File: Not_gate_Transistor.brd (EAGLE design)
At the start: 24.3 x 22.9 mm, 8 parts, among them Q1 BC547A

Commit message: update
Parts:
- moved 5V 27.9 mm to (12.1, 33.9), turned to 180 degrees
- moved S1 14.5 mm to (9.01, 25.5), turned to 90 degrees
- moved R2 9.77 mm to (15.5, 25.7), turned to 270 degrees
- moved LED1 9.52 mm to (12.6, 12.5), turned to 270 degrees
- moved Q1 9.22 mm to (13.8, 16.6)
- moved GND 3.73 mm to (8.19, 8.05)
- moved OUTPUT 3.61 mm to (15.7, 8.00)
- moved R1 1.05 mm to (8.51, 16.3)
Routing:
- net 5V: track 26.8 -> 0.00 mm
- net GND: track 24.5 -> 0.00 mm
- net N$2: track 10.4 -> 0.00 mm
- net N$3: track 10.1 -> 0.00 mm
- net N$4: track 8.37 -> 0.00 mm
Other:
- board size 24.3 x 22.9 mm -> 22 x 40 mm
- board text added: "Pinwheel Robotics"
- board text added: "care@pinwheel.in"

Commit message: New Updates
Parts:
- moved OUTPUT 0.11 mm to (15.7, 8.10)
- moved GND 0.09 mm to (8.27, 8.09)
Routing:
- net GND: track 0.00 -> 19.1 mm
- net 5V: track 0.00 -> 16.8 mm
- net N$4: track 0.00 -> 8.89 mm
- net N$2: track 0.00 -> 7.69 mm
- net N$3: track 0.00 -> 4.05 mm
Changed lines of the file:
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@@
 <drawing>
 <settings>
-<setting alwaysvectorfont="yes"/>
+<setting alwaysvectorfont="no"/>
 <setting verticaltext="up"/>
 </settings>
@@
 <plain>
 <text x="4.516" y="14.23" size="1.778" layer="21" rot="R90">Pinwheel Robotics </text>
-<hole x="3.009" y="38.751" drill="3"/>
-<hole x="20.944" y="38.738" drill="3"/>
-<hole x="3.08" y="3.04" drill="3"/>
-<hole x="20.91" y="3.088" drill="3"/>
+<hole x="3.009" y="38.5" drill="3"/>
+<hole x="21" y="38.5" drill="3"/>
+<hole x="3" y="3.04" drill="3"/>
+<hole x="21" y="3.088" drill="3"/>
 <wire x1="1" y1="39.059846875" x2="1" y2="3.00098125" width="0.1524" layer="20"/>
 <wire x1="1" y1="3.00098125" x2="3.00098125" y2="1" width="0.1524" layer="20" curve="90"/>
@@
 <attribute name="NAME" x="9.894" y="29.673" size="0.8128" layer="21" font="vector"/>
 </element>
-<element name="GND" library="microbit" package="MICROBIT_PAD" value="MICROBIT_PAD" x="8.185" y="8.052" smashed="yes">
-<attribute name="NAME" x="5.291" y="10.194" size="0.8128" layer="21" font="vector" rot="R90"/>
+<element name="GND" library="microbit" package="MICROBIT_PAD" value="MICROBIT_PAD" x="8.266084375" y="8.092525" smashed="yes">
+<attribute name="NAME" x="5.372084375" y="10.234525" size="0.8128" layer="21" font="vector" rot="R90"/>
 </element>
 <element name="LED1" library="led" library_urn="urn:adsk.eagle:library:259" package="CHIP-LED0805" package3d_urn="urn:adsk.eagle:package:15818/2" value="" x="12.603" y="12.494" smashed="yes" rot="R270">
@@
 <attribute name="VALUE" x="11.333" y="9.954" size="1.27" layer="27"/>
 </element>
-<element name="OUTPUT" library="microbit" package="MICROBIT_PAD" value="MICROBIT_PAD" x="15.686" y="8.002" smashed="yes">
-<attribute name="NAME" x="13.4" y="11.558" size="0.8128" layer="21" font="vector"/>
+<element name="OUTPUT" library="microbit" package="MICROBIT_PAD" value="MICROBIT_PAD" x="15.73645625" y="8.102915625" smashed="yes">
+<attribute name="NAME" x="13.45045625" y="11.658915625" size="0.8128" layer="21" font="vector"/>
 </element>
 <element name="Q1" library="transistor-npn" library_urn="urn:adsk.eagle:library:398" package="TO92" package3d_urn="urn:adsk.eagle:package:28523/2" value="BC547A" x="13.843" y="16.637" smashed="yes">
@@
 <contactref element="OUTPUT" pad="PAD"/>
 <contactref element="GND" pad="PAD"/>
-<wire x1="13.653" y1="12.494" x2="15.113" y2="16.637" width="0" layer="19" extent="1-1"/>
-<wire x1="8.185" y1="8.052" x2="13.653" y2="12.494" width="0" layer="19" extent="1-1"/>
-<wire x1="15.686" y1="8.002" x2="8.185" y2="8.052" width="0" layer="19" extent="1-1"/>
+<wire x1="13.8176" y1="15.24" x2="13.8176" y2="12.5984" width="0.254" layer="1"/>
+<wire x1="15.0368" y1="16.4592" x2="13.8176" y2="15.24" width="0.254" layer="1"/>
+<wire x1="13.8176" y1="12.5984" x2="13.653" y2="12.494" width="0.254" layer="1"/>
+<wire x1="15.0368" y1="16.4592" x2="15.113" y2="16.637" width="0.254" layer="1"/>
+<wire x1="13.8176" y1="9.9568" x2="13.8176" y2="12.3952" width="0.254" layer="1"/>
+<wire x1="15.6464" y1="8.128" x2="13.8176" y2="9.9568" width="0.254" layer="1"/>
+<wire x1="13.8176" y1="12.3952" x2="13.653" y2="12.494" width="0.254" layer="1"/>
+<wire x1="15.6464" y1="8.128" x2="15.73645625" y2="8.102915625" width="0.254" layer="1"/>
+<wire x1="10.7696" y1="8.128" x2="8.3312" y2="8.128" width="0.254" layer="1"/>
+<wire x1="12.5984" y1="9.9568" x2="10.7696" y2="8.128" width="0.254" layer="1"/>
+<wire x1="13.8176" y1="9.9568" x2="12.5984" y2="9.9568" width="0.254" layer="1"/>
+<wire x1="8.3312" y1="8.128" x2="8.266084375" y2="8.092525" width="0.254" layer="1"/>
+<wire x1="13.8176" y1="9.9568" x2="15.73645625" y2="8.102915625" width="0.254" layer="1"/>
 </signal>
 <signal name="N$2">
@@
 <contactref element="R1" pad="1"/>
 <contactref element="LED1" pad="A"/>
-<wire x1="11.553" y1="12.494" x2="12.573" y2="16.637" width="0" layer="19" extent="1-1"/>
-<wire x1="8.509" y1="12.514" x2="11.553" y2="12.494" width="0" layer="19" extent="1-1"/>
+<wire x1="8.5344" y1="12.5984" x2="11.3792" y2="12.5984" width="0.254" layer="1"/>
+<wire x1="11.3792" y1="12.5984" x2="11.553" y2="12.494" width="0.254" layer="1"/>
+<wire x1="8.5344" y1="12.5984" x2="8.509" y2="12.514" width="0.254" layer="1"/>
+<wire x1="12.3952" y1="13.4112" x2="12.3952" y2="16.4592" width="0.254" layer="1"/>
+<wire x1="11.5824" y1="12.5984" x2="12.3952" y2="13.4112" width="0.254" layer="1"/>
+<wire x1="12.3952" y1="16.4592" x2="12.573" y2="16.637" width="0.254" layer="1"/>
+<wire x1="11.5824" y1="12.5984" x2="11.553" y2="12.494" width="0.254" layer="1"/>
 </signal>
 <signal name="N$3">
 <contactref element="R2" pad="2"/>
 <contactref element="Q1" pad="2"/>
-<wire x1="13.843" y1="18.542" x2="15.524" y2="21.902" width="0" layer="19" extent="1-1"/>
+<wire x1="14.0208" y1="20.32" x2="14.0208" y2="18.6944" width="0.254" layer="1"/>
+<wire x1="15.4432" y1="21.7424" x2="14.0208" y2="20.32" width="0.254" layer="1"/>
+<wire x1="14.0208" y1="18.6944" x2="13.843" y2="18.542" width="0.254" layer="1"/>
+<wire x1="15.4432" y1="21.7424" x2="15.524" y2="21.902" width="0.254" layer="1"/>
 </signal>
 <signal name="N$4">
 <contactref element="S1" pad="3"/>
 <contactref element="R2" pad="1"/>
-<wire x1="15.524" y1="29.402" x2="11.2726" y2="22.2718" width="0" layer="19" extent="1-1"/>
+<wire x1="15.4432" y1="26.416" x2="15.4432" y2="29.2608" width="0.254" layer="1"/>
+<wire x1="11.3792" y1="22.352" x2="15.4432" y2="26.416" width="0.254" layer="1"/>
+<wire x1="15.4432" y1="29.2608" x2="15.524" y2="29.402" width="0.254" layer="1"/>
+<wire x1="11.3792" y1="22.352" x2="11.2726" y2="22.2718" width="0.254" layer="1"/>
 </signal>
 <signal name="5V">
@@
 <contactref element="5V" pad="PAD"/>
 <contactref element="R1" pad="2"/>
-<wire x1="8.509" y1="20.014" x2="6.7514" y2="22.2718" width="0" layer="19" extent="1-1"/>
-<wire x1="12.053" y1="33.864" x2="6.7514" y2="22.2718" width="0" layer="19" extent="1-1"/>
+<wire x1="8.3312" y1="20.7264" x2="8.3312" y2="20.1168" width="0.254" layer="1"/>
+<wire x1="6.9088" y1="22.1488" x2="8.3312" y2="20.7264" width="0.254" layer="1"/>
+<wire x1="8.3312" y1="20.1168" x2="8.509" y2="20.014" width="0.254" layer="1"/>
+<wire x1="6.9088" y1="22.1488" x2="6.7514" y2="22.2718" width="0.254" layer="1"/>
+<wire x1="6.9088" y1="27.0256" x2="6.9088" y2="22.352" width="0.254" layer="1"/>
+<wire x1="11.9888" y1="32.1056" x2="6.9088" y2="27.0256" width="0.254" layer="1"/>
+<wire x1="11.9888" y1="33.7312" x2="11.9888" y2="32.1056" width="0.254" layer="1"/>
+<wire x1="6.9088" y1="22.352" x2="6.7514" y2="22.2718" width="0.254" layer="1"/>
+<wire x1="11.9888" y1="33.7312" x2="12.053" y2="33.864" width="0.254" layer="1"/>
 </signal>
 </signals>

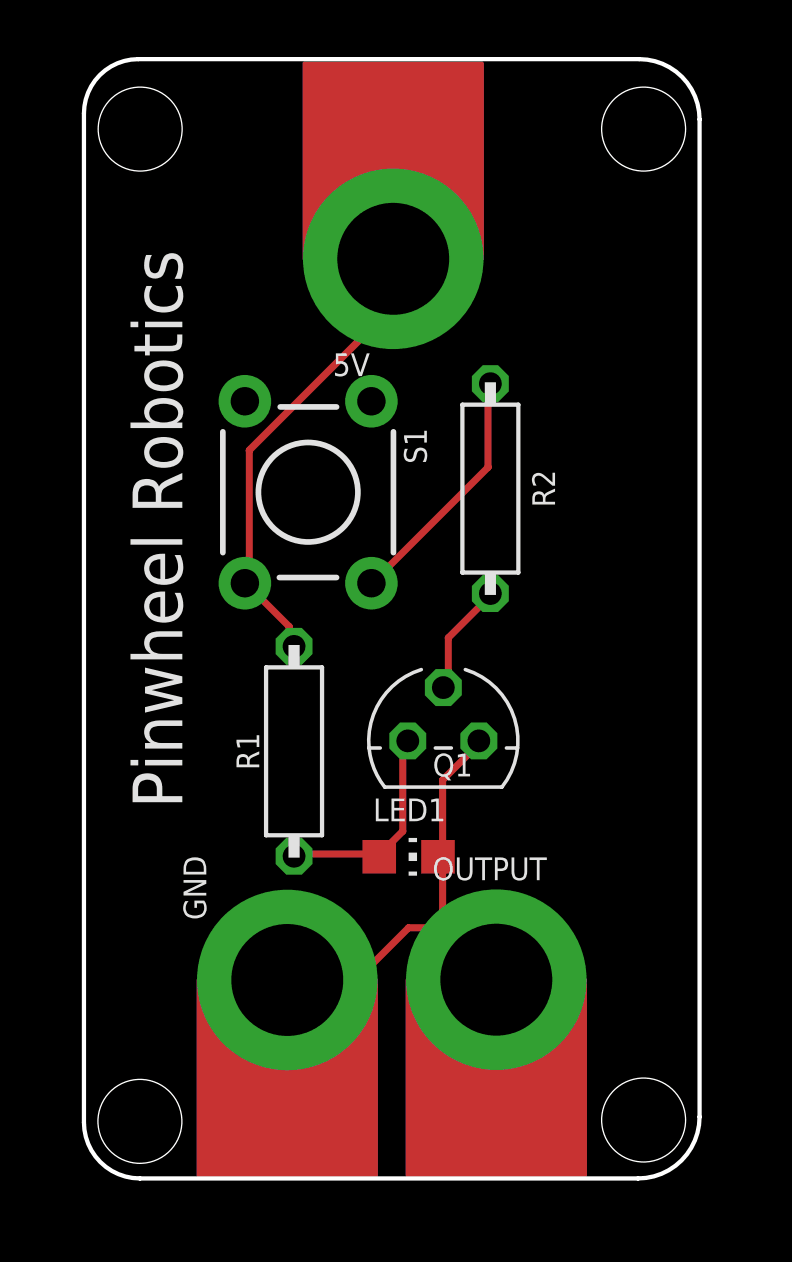
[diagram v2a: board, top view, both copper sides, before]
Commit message: New Update for board curv
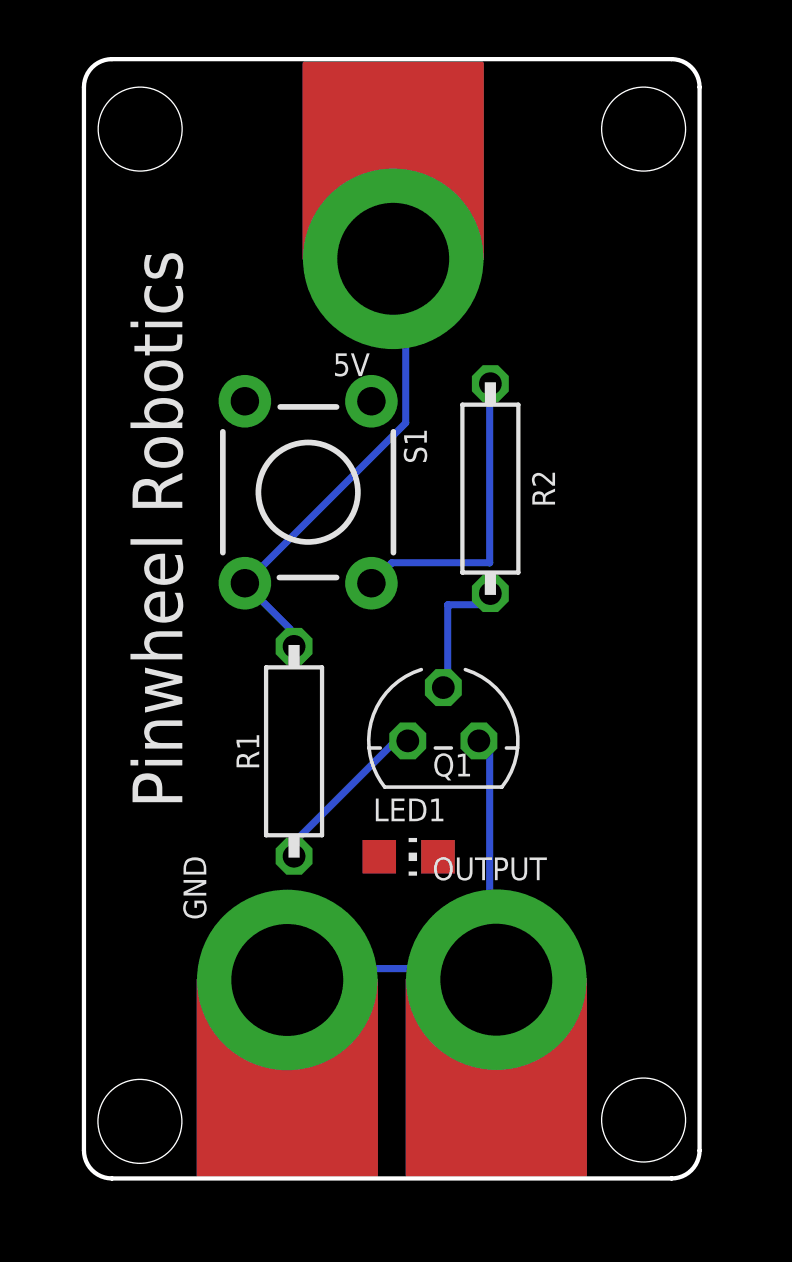
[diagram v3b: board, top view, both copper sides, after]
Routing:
- net GND: track 19.1 -> 16.3 mm
- net N$4: track 8.89 -> 10.9 mm
- net N$2: track 7.69 -> 6.09 mm
- net N$3: track 4.05 -> 4.89 mm
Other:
- outline, holes or cut-outs redrawn
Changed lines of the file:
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@@
 <drawing>
 <settings>
-<setting alwaysvectorfont="no"/>
+<setting alwaysvectorfont="yes"/>
 <setting verticaltext="up"/>
 </settings>
@@
 <hole x="3" y="3.04" drill="3"/>
 <hole x="21" y="3.088" drill="3"/>
-<wire x1="1" y1="39.059846875" x2="1" y2="3.00098125" width="0.1524" layer="20"/>
-<wire x1="1" y1="3.00098125" x2="3.00098125" y2="1" width="0.1524" layer="20" curve="90"/>
-<wire x1="3.00098125" y1="1" x2="20.79976875" y2="1" width="0.1524" layer="20"/>
-<wire x1="20.79976875" y1="1" x2="23" y2="3.20023125" width="0.1524" layer="20" curve="90"/>
-<wire x1="23" y1="3.20023125" x2="23" y2="38.845959375" width="0.1524" layer="20"/>
-<wire x1="23" y1="38.845959375" x2="20.845959375" y2="41" width="0.1524" layer="20" curve="90"/>
-<wire x1="20.845959375" y1="41" x2="2.940153125" y2="41" width="0.1524" layer="20"/>
-<wire x1="2.940153125" y1="41" x2="1" y2="39.059846875" width="0.1524" layer="20" curve="90"/>
+<wire x1="2" y1="1" x2="22" y2="1" width="0.1524" layer="20"/>
+<wire x1="22" y1="1" x2="23" y2="2" width="0.1524" layer="20" curve="90"/>
+<wire x1="23" y1="2" x2="23" y2="40" width="0.1524" layer="20"/>
+<wire x1="23" y1="40" x2="22" y2="41" width="0.1524" layer="20" curve="90"/>
+<wire x1="22" y1="41" x2="2" y2="41" width="0.1524" layer="20"/>
+<wire x1="2" y1="41" x2="1" y2="40" width="0.1524" layer="20" curve="90"/>
+<wire x1="1" y1="40" x2="1" y2="2" width="0.1524" layer="20"/>
+<wire x1="1" y1="2" x2="2" y2="1" width="0.1524" layer="20" curve="90"/>
 <text x="21" y="34.5" size="1.778" layer="22" rot="MR270">care@pinwheel.in</text>
 </plain>
@@
 <param name="TopRouterVariant" value="1"/>
 <param name="tpViaShape" value="round"/>
-<param name="PrefDir.1" value="a"/>
+<param name="PrefDir.1" value="0"/>
 <param name="PrefDir.2" value="0"/>
 <param name="PrefDir.3" value="0"/>
@@
 <contactref element="OUTPUT" pad="PAD"/>
 <contactref element="GND" pad="PAD"/>
-<wire x1="13.8176" y1="15.24" x2="13.8176" y2="12.5984" width="0.254" layer="1"/>
-<wire x1="15.0368" y1="16.4592" x2="13.8176" y2="15.24" width="0.254" layer="1"/>
-<wire x1="13.8176" y1="12.5984" x2="13.653" y2="12.494" width="0.254" layer="1"/>
-<wire x1="15.0368" y1="16.4592" x2="15.113" y2="16.637" width="0.254" layer="1"/>
-<wire x1="13.8176" y1="9.9568" x2="13.8176" y2="12.3952" width="0.254" layer="1"/>
-<wire x1="15.6464" y1="8.128" x2="13.8176" y2="9.9568" width="0.254" layer="1"/>
-<wire x1="13.8176" y1="12.3952" x2="13.653" y2="12.494" width="0.254" layer="1"/>
-<wire x1="15.6464" y1="8.128" x2="15.73645625" y2="8.102915625" width="0.254" layer="1"/>
-<wire x1="10.7696" y1="8.128" x2="8.3312" y2="8.128" width="0.254" layer="1"/>
-<wire x1="12.5984" y1="9.9568" x2="10.7696" y2="8.128" width="0.254" layer="1"/>
-<wire x1="13.8176" y1="9.9568" x2="12.5984" y2="9.9568" width="0.254" layer="1"/>
-<wire x1="8.3312" y1="8.128" x2="8.266084375" y2="8.092525" width="0.254" layer="1"/>
-<wire x1="13.8176" y1="9.9568" x2="15.73645625" y2="8.102915625" width="0.254" layer="1"/>
+<wire x1="15.5" y1="8.5" x2="15.5" y2="16.5" width="0.254" layer="16"/>
+<wire x1="15.5" y1="16.5" x2="15.113" y2="16.637" width="0.254" layer="16"/>
+<wire x1="15.5" y1="8.5" x2="8.5" y2="8.5" width="0.254" layer="16"/>
+<wire x1="8.5" y1="8.5" x2="8.266084375" y2="8.092525" width="0.254" layer="16"/>
+<wire x1="15.5" y1="8.5" x2="15.73645625" y2="8.102915625" width="0.254" layer="16"/>
+<wire x1="15.113" y1="16.637" x2="13.653" y2="12.494" width="0" layer="19" extent="1-1"/>
 </signal>
 <signal name="N$2">
@@
 <contactref element="R1" pad="1"/>
 <contactref element="LED1" pad="A"/>
-<wire x1="8.5344" y1="12.5984" x2="11.3792" y2="12.5984" width="0.254" layer="1"/>
-<wire x1="11.3792" y1="12.5984" x2="11.553" y2="12.494" width="0.254" layer="1"/>
-<wire x1="8.5344" y1="12.5984" x2="8.509" y2="12.514" width="0.254" layer="1"/>
-<wire x1="12.3952" y1="13.4112" x2="12.3952" y2="16.4592" width="0.254" layer="1"/>
-<wire x1="11.5824" y1="12.5984" x2="12.3952" y2="13.4112" width="0.254" layer="1"/>
-<wire x1="12.3952" y1="16.4592" x2="12.573" y2="16.637" width="0.254" layer="1"/>
-<wire x1="11.5824" y1="12.5984" x2="11.553" y2="12.494" width="0.254" layer="1"/>
+<wire x1="12" y1="16.5" x2="8.5" y2="13" width="0.254" layer="16"/>
+<wire x1="12.5" y1="16.5" x2="12" y2="16.5" width="0.254" layer="16"/>
+<wire x1="8.5" y1="13" x2="8.509" y2="12.514" width="0.254" layer="16"/>
+<wire x1="12.5" y1="16.5" x2="12.573" y2="16.637" width="0.254" layer="16"/>
+<wire x1="8.509" y1="12.514" x2="11.553" y2="12.494" width="0" layer="19" extent="1-1"/>
 </signal>
 <signal name="N$3">
 <contactref element="R2" pad="2"/>
 <contactref element="Q1" pad="2"/>
-<wire x1="14.0208" y1="20.32" x2="14.0208" y2="18.6944" width="0.254" layer="1"/>
-<wire x1="15.4432" y1="21.7424" x2="14.0208" y2="20.32" width="0.254" layer="1"/>
-<wire x1="14.0208" y1="18.6944" x2="13.843" y2="18.542" width="0.254" layer="1"/>
-<wire x1="15.4432" y1="21.7424" x2="15.524" y2="21.902" width="0.254" layer="1"/>
+<wire x1="14" y1="21.5" x2="14" y2="19" width="0.254" layer="16"/>
+<wire x1="15.5" y1="21.5" x2="14" y2="21.5" width="0.254" layer="16"/>
+<wire x1="14" y1="19" x2="13.843" y2="18.542" width="0.254" layer="16"/>
+<wire x1="15.5" y1="21.5" x2="15.524" y2="21.902" width="0.254" layer="16"/>
 </signal>
 <signal name="N$4">
 <contactref element="S1" pad="3"/>
 <contactref element="R2" pad="1"/>
-<wire x1="15.4432" y1="26.416" x2="15.4432" y2="29.2608" width="0.254" layer="1"/>
-<wire x1="11.3792" y1="22.352" x2="15.4432" y2="26.416" width="0.254" layer="1"/>
-<wire x1="15.4432" y1="29.2608" x2="15.524" y2="29.402" width="0.254" layer="1"/>
-<wire x1="11.3792" y1="22.352" x2="11.2726" y2="22.2718" width="0.254" layer="1"/>
+<wire x1="15.5" y1="23" x2="15.5" y2="29" width="0.254" layer="16"/>
+<wire x1="12" y1="23" x2="15.5" y2="23" width="0.254" layer="16"/>
+<wire x1="11.5" y1="22.5" x2="12" y2="23" width="0.254" layer="16"/>
+<wire x1="15.5" y1="29" x2="15.524" y2="29.402" width="0.254" layer="16"/>
+<wire x1="11.5" y1="22.5" x2="11.2726" y2="22.2718" width="0.254" layer="16"/>
 </signal>
 <signal name="5V">
@@
 <contactref element="5V" pad="PAD"/>
 <contactref element="R1" pad="2"/>
-<wire x1="8.3312" y1="20.7264" x2="8.3312" y2="20.1168" width="0.254" layer="1"/>
-<wire x1="6.9088" y1="22.1488" x2="8.3312" y2="20.7264" width="0.254" layer="1"/>
-<wire x1="8.3312" y1="20.1168" x2="8.509" y2="20.014" width="0.254" layer="1"/>
-<wire x1="6.9088" y1="22.1488" x2="6.7514" y2="22.2718" width="0.254" layer="1"/>
-<wire x1="6.9088" y1="27.0256" x2="6.9088" y2="22.352" width="0.254" layer="1"/>
-<wire x1="11.9888" y1="32.1056" x2="6.9088" y2="27.0256" width="0.254" layer="1"/>
-<wire x1="11.9888" y1="33.7312" x2="11.9888" y2="32.1056" width="0.254" layer="1"/>
-<wire x1="6.9088" y1="22.352" x2="6.7514" y2="22.2718" width="0.254" layer="1"/>
-<wire x1="11.9888" y1="33.7312" x2="12.053" y2="33.864" width="0.254" layer="1"/>
+<wire x1="7" y1="22" x2="8.5" y2="20.5" width="0.254" layer="16"/>
+<wire x1="8.5" y1="20.5" x2="8.509" y2="20.014" width="0.254" layer="16"/>
+<wire x1="7" y1="22" x2="6.7514" y2="22.2718" width="0.254" layer="16"/>
+<wire x1="12.5" y1="28" x2="7" y2="22.5" width="0.254" layer="16"/>
+<wire x1="12.5" y1="33.5" x2="12.5" y2="28" width="0.254" layer="16"/>
+<wire x1="7" y1="22.5" x2="6.7514" y2="22.2718" width="0.254" layer="16"/>
+<wire x1="12.5" y1="33.5" x2="12.053" y2="33.864" width="0.254" layer="16"/>
 </signal>
 </signals>
